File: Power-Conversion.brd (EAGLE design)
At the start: 182.9 x 114.3 mm, 46 parts, among them Q1 SUM90P10-19L, U7 LM2678

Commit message: Stuff
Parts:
- moved U$7 2.04 mm to (163.3, 28.1)
- moved U$5 0.38 mm to (162.4, 33.5)
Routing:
- net ON/OFF: track 169.5 -> 173.3 mm
- net N$10: track 6.11 -> 7.96 mm
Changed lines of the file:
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@@
 <attribute name="PN-DIGI" value="BZX84C22LT1GOSCT-ND" x="165.1" y="19.05" size="1.778" layer="27" rot="R180" display="off"/>
 </element>
-<element name="U$5" library="MotherboardParts" package="SOT23-3" value="5V" x="162.052" y="33.528" rot="R90"/>
+<element name="U$5" library="MotherboardParts" package="SOT23-3" value="5V" x="162.433" y="33.528" rot="R90"/>
 <element name="U$6" library="MotherboardParts" package="SOT23-3" value="22V" x="164.084" y="15.24" rot="R180">
 <attribute name="PN-DIGI" value="BZX84C22LT1GOSCT-ND" x="164.084" y="15.24" size="1.778" layer="27" rot="R180" display="off"/>
 </element>
-<element name="U$7" library="MotherboardParts" package="DPAK" value="NMOSFET-DPAK" x="161.29" y="28.194" rot="R90">
-<attribute name="PN-DIGI" value="497-4329-1-ND" x="161.29" y="28.194" size="1.778" layer="27" rot="R90" display="off"/>
-<attribute name="VDSS" value="60V" x="161.29" y="28.194" size="1.778" layer="27" rot="R90" display="off"/>
+<element name="U$7" library="MotherboardParts" package="DPAK" value="NMOSFET-DPAK" x="163.322" y="28.067" rot="R90">
+<attribute name="PN-DIGI" value="497-4329-1-ND" x="163.322" y="28.067" size="1.778" layer="27" rot="R90" display="off"/>
+<attribute name="VDSS" value="60V" x="163.322" y="28.067" size="1.778" layer="27" rot="R90" display="off"/>
 </element>
 <element name="U$9" library="PowerComponents" package="DPAK-3" value="SWITCHMODE_SCHOTTKY" x="8.382" y="58.42" rot="MR270"/>
@@
 <wire x1="181.356" y1="23.114" x2="181.356" y2="24.384" width="0.6096" layer="16"/>
 <via x="181.356" y="24.384" extent="1-16" drill="0.35"/>
-<wire x1="181.356" y1="24.384" x2="181.356" y2="26.924" width="0.6096" layer="1"/>
-<wire x1="181.356" y1="26.924" x2="180.086" y2="28.194" width="0.6096" layer="1"/>
 <via x="180.086" y="31.242" extent="1-16" drill="0.35"/>
-<wire x1="180.086" y1="28.194" x2="180.086" y2="31.242" width="0.6096" layer="1"/>
 <polygon width="0.4064" layer="16">
 <vertex x="28.448" y="96.52"/>
@@
 <contactref element="U$8" pad="P$11"/>
 <contactref element="U$8" pad="P$10"/>
+<wire x1="181.356" y1="27.94" x2="180.086" y2="29.21" width="0.6096" layer="1"/>
+<wire x1="180.086" y1="29.21" x2="180.086" y2="31.242" width="0.6096" layer="1"/>
+<wire x1="181.356" y1="24.384" x2="181.356" y2="27.94" width="0.6096" layer="1"/>
 </signal>
 <signal name="N$9">
@@
 <contactref element="R1" pad="2"/>
 <contactref element="U$7" pad="1"/>
-<wire x1="166.6" y1="25.914" x2="166.028" y2="25.342" width="0.8128" layer="1"/>
-<wire x1="166.028" y1="25.342" x2="166.028" y2="22.352" width="0.8128" layer="1"/>
 <wire x1="166.028" y1="22.352" x2="166.028" y2="20.072" width="0.8128" layer="1"/>
 <wire x1="166.028" y1="20.072" x2="166.05" y2="20.05" width="0.8128" layer="1"/>
+<wire x1="165.989" y1="22.391" x2="166.028" y2="22.352" width="0.4064" layer="1"/>
+<wire x1="168.632" y1="25.787" x2="168.626" y2="25.781" width="0.8128" layer="1"/>
+<wire x1="168.626" y1="25.781" x2="166.751" y2="25.781" width="0.8128" layer="1"/>
+<wire x1="166.751" y1="25.781" x2="165.989" y2="25.019" width="0.8128" layer="1"/>
+<wire x1="165.989" y1="25.019" x2="165.989" y2="22.391" width="0.8128" layer="1"/>
 </signal>
 <signal name="+5V">
@@
 <vertex x="179.578" y="14.224"/>
 <vertex x="179.832" y="14.478"/>
-<vertex x="179.832" y="27.178"/>
-<vertex x="176.022" y="27.178"/>
-<vertex x="170.434" y="32.766"/>
+<vertex x="180.086" y="28.194"/>
+<vertex x="173.863" y="35.052"/>
 <vertex x="169.926" y="33.274"/>
-<vertex x="162.306" y="33.274"/>
-<vertex x="162.306" y="31.75"/>
-<vertex x="164.084" y="29.972"/>
+<vertex x="163.068" y="33.274"/>
+<vertex x="163.068" y="31.75"/>
+<vertex x="164.719" y="31.75"/>
+<vertex x="164.846" y="31.623"/>
 <vertex x="164.846" y="29.21"/>
 <vertex x="167.386" y="29.21"/>
 <vertex x="169.418" y="27.178"/>
-<vertex x="169.418" y="23.622"/>
-<vertex x="167.894" y="23.622"/>
+<vertex x="170.561" y="27.305"/>
+<vertex x="170.561" y="24.765"/>
+<vertex x="170.434" y="24.638"/>
 </polygon>
 <via x="140.462" y="4.318" extent="1-16" drill="0.35"/>
@@
 <wire x1="139.192" y1="3.302" x2="139.192" y2="2.032" width="0.8128" layer="1"/>
 <polygon width="0.4064" layer="1">
-<vertex x="35.052" y="23.368"/>
+<vertex x="35.052" y="24.13"/>
 <vertex x="35.052" y="12.954"/>
 <vertex x="35.306" y="12.7"/>
 <vertex x="155.448" y="12.7"/>
-<vertex x="156.718" y="13.97"/>
-<vertex x="159.004" y="16.256"/>
-<vertex x="159.004" y="17.526"/>
+<vertex x="157.988" y="12.954"/>
+<vertex x="159.004" y="13.97"/>
 <vertex x="159.004" y="22.86"/>
-<vertex x="155.448" y="26.416"/>
-<vertex x="155.448" y="32.258"/>
-<vertex x="159.258" y="36.068"/>
+<vertex x="157.988" y="26.416"/>
+<vertex x="157.988" y="32.258"/>
 <vertex x="159.512" y="36.322"/>
 <vertex x="164.338" y="36.322"/>
 <vertex x="164.338" y="32.766"/>
 <vertex x="169.164" y="32.766"/>
-<vertex x="173.482" y="28.448"/>
-<vertex x="173.482" y="42.164"/>
-<vertex x="158.75" y="42.164"/>
-<vertex x="151.638" y="35.052"/>
+<vertex x="174.879" y="28.448"/>
+<vertex x="174.879" y="42.164"/>
+<vertex x="146.431" y="42.164"/>
+<vertex x="146.431" y="29.464"/>
+<vertex x="151.638" y="24.257"/>
 <vertex x="151.638" y="19.05"/>
 <vertex x="151.384" y="18.796"/>
@@
 <vertex x="39.878" y="18.796"/>
 <vertex x="39.878" y="24.13"/>
-<vertex x="35.052" y="24.13"/>
 </polygon>
 <contactref element="U$20" pad="48V_GND4"/>
@@
 <contactref element="R2" pad="1"/>
 <contactref element="U$5" pad="3"/>
-<wire x1="160.952" y1="33.528" x2="160.952" y2="29.444" width="0.6096" layer="1"/>
-<wire x1="159.988" y1="28.48" x2="160.952" y2="29.444" width="0.6096" layer="1"/>
-<wire x1="159.988" y1="28.48" x2="159.702" y2="28.194" width="0.6096" layer="1"/>
-<wire x1="160.782" y1="15.836" x2="160.782" y2="27.686" width="0.6096" layer="1"/>
+<wire x1="160.952" y1="29.444" x2="159.988" y2="28.48" width="0.6096" layer="1"/>
+<wire x1="159.988" y1="28.48" x2="161.734" y2="28.067" width="0.6096" layer="1"/>
 <wire x1="160.782" y1="27.686" x2="159.988" y2="28.48" width="0.6096" layer="1"/>
-<wire x1="159.702" y1="28.194" x2="159.702" y2="24.828" width="0.4064" layer="1"/>
-<wire x1="159.702" y1="24.828" x2="159.258" y2="24.384" width="0.4064" layer="1"/>
 <via x="159.258" y="24.384" extent="1-16" drill="0.35"/>
 <wire x1="159.258" y1="24.384" x2="152.908" y2="24.384" width="0.4064" layer="16"/>
@@
 <wire x1="33.4344" y1="24.2904" x2="42.1156125" y2="24.2904" width="0.4064" layer="16"/>
 <wire x1="42.4632125" y1="24.638" x2="55.626" y2="24.638" width="0.4064" layer="16"/>
+<wire x1="159.702" y1="26.606" x2="160.782" y2="27.686" width="0.4064" layer="1"/>
+<wire x1="160.782" y1="25.908" x2="160.782" y2="27.686" width="0.4064" layer="1"/>
+<wire x1="159.258" y1="24.384" x2="160.782" y2="25.908" width="0.4064" layer="1"/>
+<wire x1="160.782" y1="15.836" x2="160.782" y2="24.13" width="0.4064" layer="1"/>
+<wire x1="161.734" y1="25.082" x2="161.734" y2="28.067" width="0.4064" layer="1"/>
+<wire x1="160.782" y1="24.13" x2="161.734" y2="25.082" width="0.4064" layer="1"/>
+<wire x1="161.333" y1="33.528" x2="161.333" y2="29.825" width="0.4064" layer="1"/>
+<wire x1="161.333" y1="29.825" x2="160.952" y2="29.444" width="0.4064" layer="1"/>
 </signal>
 <signal name="+12V_1">

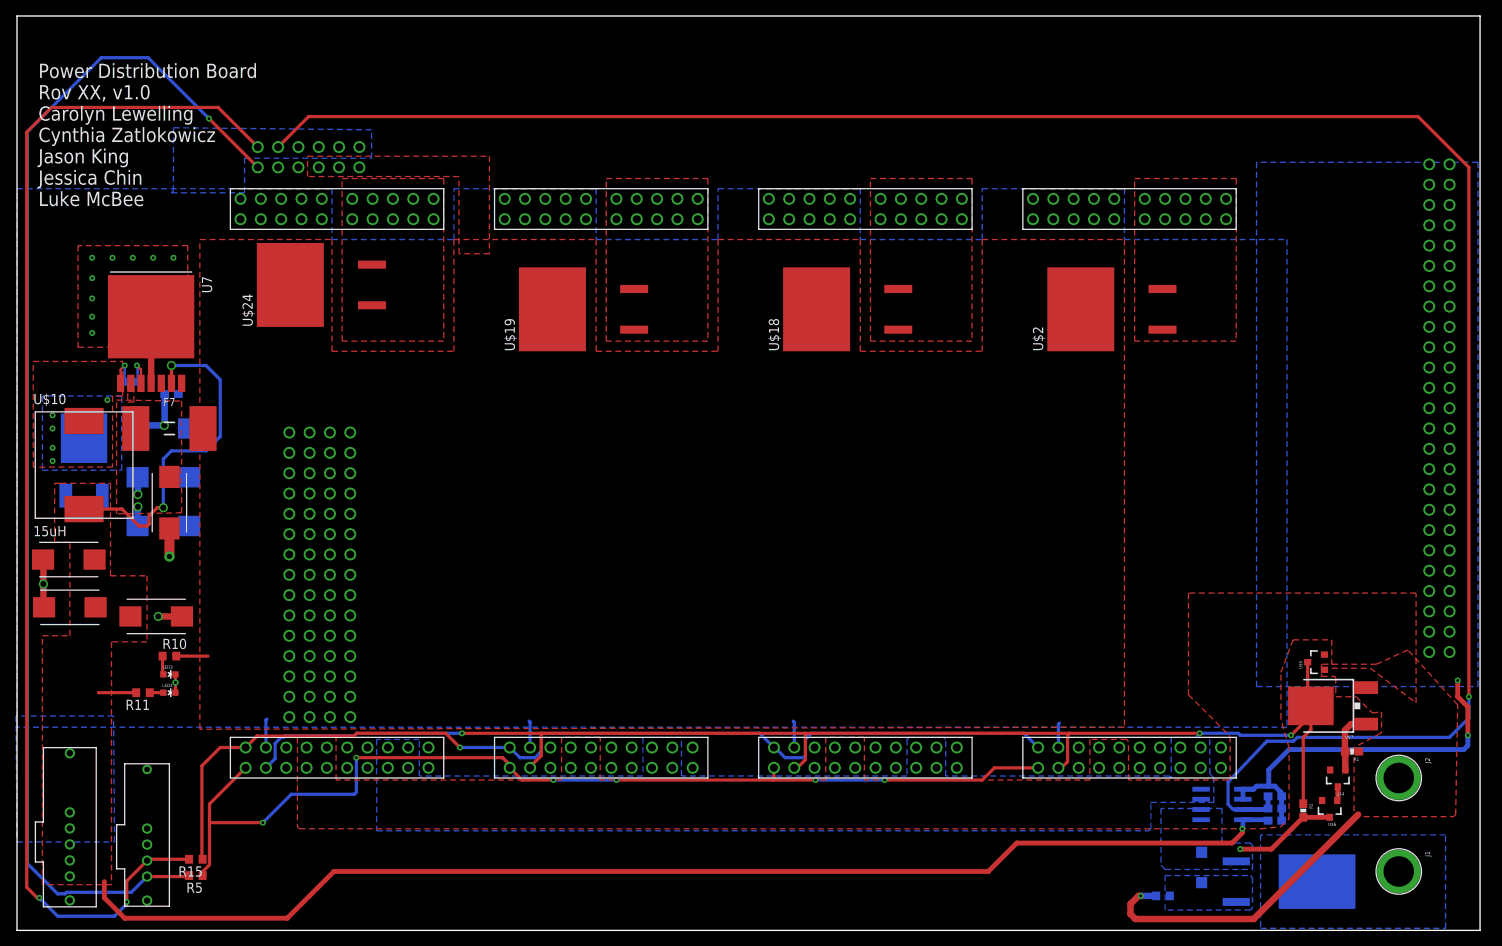
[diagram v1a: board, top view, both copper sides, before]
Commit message: Fixed trace widths for +48V and GND
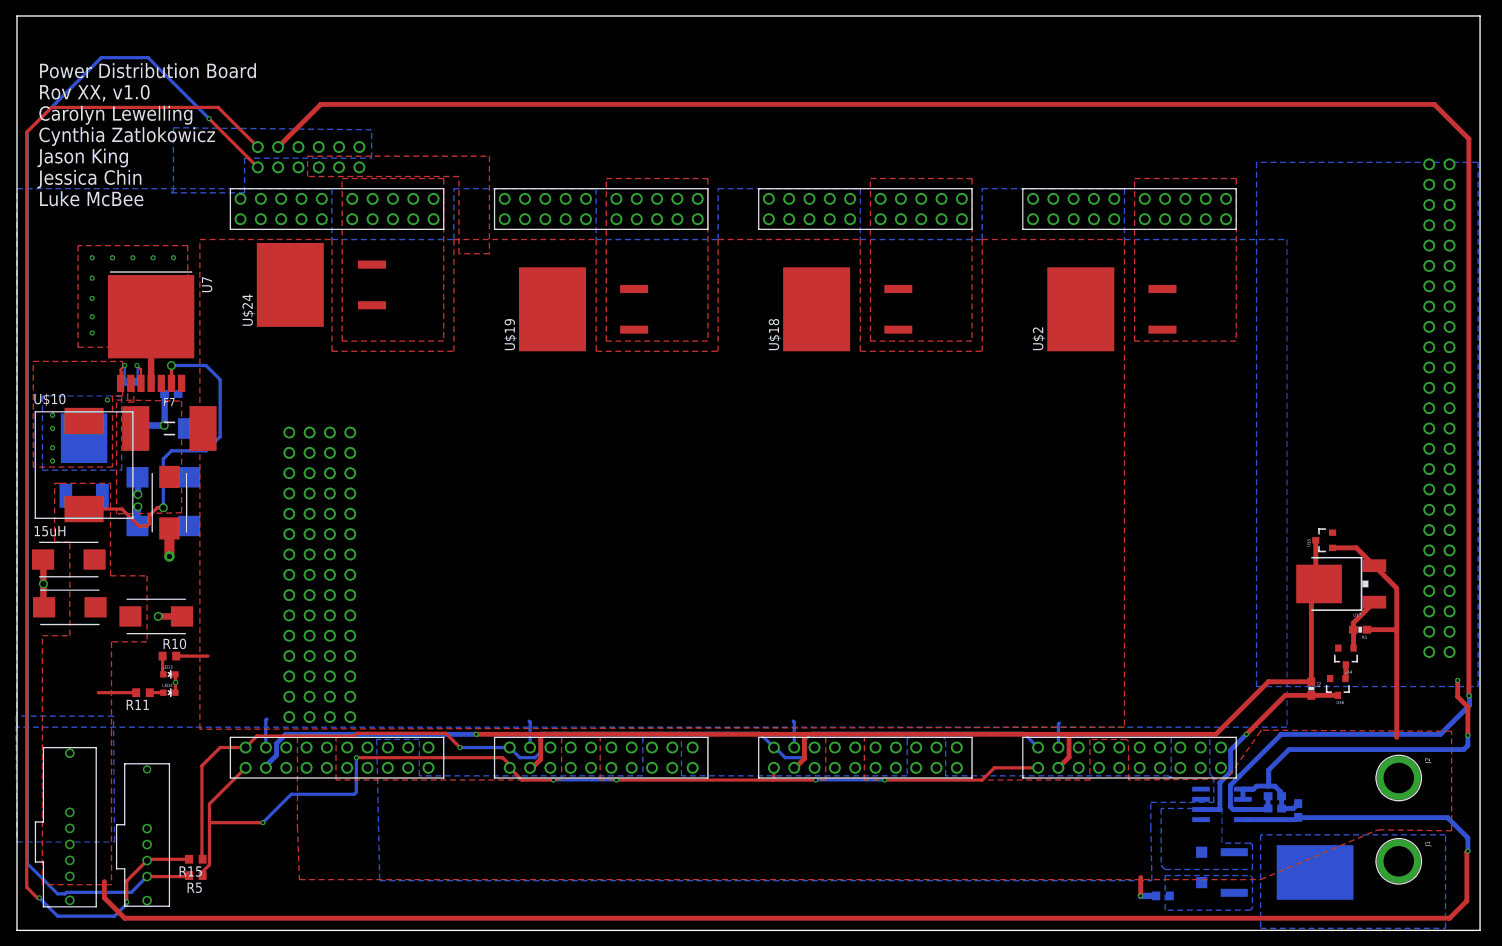
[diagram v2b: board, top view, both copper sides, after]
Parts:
- moved U$5 15.3 mm to (163.4, 48.8)
- moved U$7 15.3 mm to (164.3, 43.3)
- moved U$6 15.3 mm to (165.1, 30.5)
- moved R1 15.3 mm to (167.9, 37.6)
- moved R2 15.3 mm to (161.8, 30.2)
- moved U$4 15.3 mm to (166.1, 34.3)
- moved C1 3.19 mm to (160.1, 15.0), turned to 270 degrees
- moved J1 1.27 mm to (172.7, 8.64)
- moved Q1 1.17 mm to (158.8, 7.24)
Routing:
- net +5V: track 202.3 -> 259.1 mm
- net +48V: track 12.8 -> 26.6 mm
- net ON/OFF: track 173.3 -> 168.9 mm, vias 3 -> 1
- net 48_I_ANALOG: track 265.1 -> 268.0 mm
- net 48V_GND: track 39.0 -> 36.8 mm
- net N$10: track 7.96 -> 6.82 mm
- net GND: track 83.5 -> 84.3 mm

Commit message: Cleaning up
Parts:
- added JP1, JP2: (no value), pinhead:1X01
- moved R15 2.33 mm to (24.5, 9.78)
- moved R5 2.16 mm to (24.5, 6.73)
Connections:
- net SCL: now also JP1.1
- net SDA: now also JP2.1
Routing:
- net SCL1: track 128.7 -> 123.5 mm
- net SDA1: track 126.2 -> 122.5 mm
- net SDA: track 153.0 -> 155.5 mm
- net SCL: track 152.5 -> 154.7 mm
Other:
- board text added: "+48V"
- board text added: "GND"
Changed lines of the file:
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@@
 Jessica Chin
 Luke McBee</text>
+<text x="176.403" y="18.415" size="1.778" layer="21">GND</text>
+<text x="176.149" y="7.112" size="1.778" layer="21">+48V</text>
 </plain>
 <attributes>
@@
 <attribute name="SPICEPREFIX" value="B" x="38.354" y="75.438" size="1.778" layer="27" rot="R90" display="off"/>
 </element>
-<element name="R15" library="resistor" package="R0603" value="0R" x="22.352" y="8.89" rot="R180"/>
-<element name="R5" library="resistor" package="R0603" value="0R" x="22.352" y="6.858" rot="R180"/>
+<element name="R15" library="resistor" package="R0603" value="0R" x="24.511" y="9.779" rot="R180"/>
+<element name="R5" library="resistor" package="R0603" value="0R" x="24.511" y="6.731" rot="R180"/>
 <element name="U$11" library="BackplaneParts" package="T2I5P" value="T2I5P" x="3.302" y="3.048" rot="R270"/>
 <element name="U$12" library="BackplaneParts" package="T2I" value="T2I" x="13.462" y="20.828" rot="R270"/>
@@
 <element name="F7" library="PowerComponents" package="PTC-2920" value="10A" x="19.05" y="62.738"/>
 <element name="U$8" library="MotherboardParts" package="ESC-FULL" value="ESC-FULL" x="36.449" y="96.647"/>
+<element name="JP1" library="pinhead" library_urn="urn:adsk.eagle:library:325" package="1X01" package3d_urn="urn:adsk.eagle:package:22485/2" value="" x="20.955" y="6.731"/>
+<element name="JP2" library="pinhead" library_urn="urn:adsk.eagle:library:325" package="1X01" package3d_urn="urn:adsk.eagle:package:22485/2" value="" x="20.955" y="9.779"/>
 </elements>
 <signals>
@@
 <contactref element="R5" pad="2"/>
 <contactref element="U$12" pad="4"/>
-<wire x1="21.502" y1="6.858" x2="21.372" y2="6.728" width="0.4064" layer="1"/>
-<wire x1="21.372" y1="6.728" x2="16.262" y2="6.728" width="0.4064" layer="1"/>
 <wire x1="1.27" y1="8.382" x2="5.08" y2="4.572" width="0.4064" layer="16"/>
 <wire x1="5.08" y1="4.572" x2="5.99820625" y2="4.572" width="0.4064" layer="16"/>
@@
 <wire x1="24.003" y1="101.473" x2="16.383" y2="109.093" width="0.4064" layer="16"/>
 <wire x1="30.099" y1="95.377" x2="24.003" y2="101.473" width="0.4064" layer="1"/>
+<contactref element="JP1" pad="1"/>
+<wire x1="16.262" y1="6.728" x2="20.952" y2="6.728" width="0.4064" layer="1"/>
+<wire x1="20.952" y1="6.728" x2="20.955" y2="6.731" width="0.4064" layer="1"/>
+<wire x1="20.955" y1="6.731" x2="23.661" y2="6.731" width="0.4064" layer="1"/>
 </signal>
 <signal name="SDA">
 <contactref element="R15" pad="2"/>
 <contactref element="U$12" pad="3"/>
-<wire x1="21.502" y1="8.89" x2="16.424" y2="8.89" width="0.4064" layer="1"/>
-<wire x1="16.424" y1="8.89" x2="16.262" y2="8.728" width="0.4064" layer="1"/>
 <wire x1="16.262" y1="8.728" x2="13.716" y2="6.182" width="0.4064" layer="1"/>
 <wire x1="13.716" y1="6.182" x2="13.716" y2="3.556" width="0.4064" layer="1"/>
@@
 <wire x1="30.099" y1="97.917" x2="25.146" y2="102.87" width="0.4064" layer="1"/>
 <wire x1="25.146" y1="102.87" x2="4.318" y2="102.87" width="0.4064" layer="1"/>
+<contactref element="JP2" pad="1"/>
+<wire x1="16.262" y1="8.728" x2="17.313" y2="9.779" width="0.4064" layer="1"/>
+<wire x1="17.313" y1="9.779" x2="20.955" y2="9.779" width="0.4064" layer="1"/>
+<wire x1="20.955" y1="9.779" x2="23.661" y2="9.779" width="0.4064" layer="1"/>
 </signal>
 <signal name="48_I_ANALOG">
@@
 <wire x1="30.0054" y1="24.2904" x2="28.575" y2="22.86" width="0.4064" layer="1"/>
 <wire x1="42.1156125" y1="24.2904" x2="30.0054" y2="24.2904" width="0.4064" layer="1"/>
-<wire x1="28.575" y1="22.86" x2="25.4" y2="22.86" width="0.4064" layer="1"/>
-<wire x1="25.4" y1="22.86" x2="23.114" y2="20.574" width="0.4064" layer="1"/>
-<wire x1="23.114" y1="8.978" x2="23.202" y2="8.89" width="0.4064" layer="1"/>
-<wire x1="23.114" y1="20.574" x2="23.114" y2="8.978" width="0.4064" layer="1"/>
+<wire x1="25.361" y1="9.779" x2="25.361" y2="19.646" width="0.4064" layer="1"/>
+<wire x1="25.361" y1="19.646" x2="28.575" y2="22.86" width="0.4064" layer="1"/>
 </signal>
 <signal name="SCL1">
@@
 <contactref element="R5" pad="1"/>
 <contactref element="U$23" pad="SCL"/>
-<wire x1="23.202" y1="6.858" x2="23.202" y2="7.33710625" width="0.4064" layer="1"/>
-<wire x1="23.202" y1="7.33710625" x2="24.0576" y2="8.19270625" width="0.4064" layer="1"/>
-<wire x1="24.0576" y1="15.8026" x2="28.575" y2="20.32" width="0.4064" layer="1"/>
-<wire x1="24.0576" y1="8.19270625" x2="24.0576" y2="13.462" width="0.4064" layer="1"/>
-<wire x1="24.0576" y1="13.462" x2="24.0576" y2="15.8026" width="0.4064" layer="1"/>
 <via x="30.734" y="13.462" extent="1-16" drill="0.35"/>
 <wire x1="30.734" y1="13.462" x2="34.29" y2="17.018" width="0.4064" layer="16"/>
@@
 <wire x1="60.706" y1="21.59" x2="61.595" y2="20.701" width="0.4064" layer="1"/>
 <wire x1="61.595" y1="20.701" x2="61.595" y2="20.32" width="0.4064" layer="1"/>
-<wire x1="24.0576" y1="13.462" x2="30.734" y2="13.462" width="0.4064" layer="1"/>
 <wire x1="42.418" y1="17.272" x2="42.418" y2="21.59" width="0.4064" layer="16"/>
 <wire x1="42.418" y1="21.59" x2="60.706" y2="21.59" width="0.4064" layer="1"/>
@@
 <wire x1="94.488" y1="18.796" x2="99.822" y2="18.796" width="0.4064" layer="1"/>
 <wire x1="99.822" y1="18.796" x2="108.458" y2="18.796" width="0.4064" layer="16"/>
+<wire x1="28.575" y1="20.32" x2="28.575" y2="13.462" width="0.4064" layer="1"/>
+<wire x1="28.575" y1="13.462" x2="30.734" y2="13.462" width="0.4064" layer="1"/>
+<wire x1="28.575" y1="13.462" x2="28.575" y2="9.945" width="0.4064" layer="1"/>
+<wire x1="28.575" y1="9.945" x2="25.361" y2="6.731" width="0.4064" layer="1"/>
 </signal>
 <signal name="N$2">
@@
 which will not be processed correctly with this version.
 </note>
+<note version="8.2" severity="warning">
+Since Version 8.2, EAGLE supports online libraries. The ids
+of those online libraries will not be understood (or retained)
+with this version.
+</note>
+<note version="8.3" severity="warning">
+Since Version 8.3, EAGLE supports URNs for individual library
+assets (packages, symbols, and devices). The URNs of those assets
+will not be understood (or retained) with this version.
+</note>
+<note version="8.3" severity="warning">
+Since Version 8.3, EAGLE supports the association of 3D packages
+with devices in libraries, schematics, and board files. Those 3D
+packages will not be understood (or retained) with this version.
+</note>
 </compatibility>

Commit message: Version submitted to elecrow
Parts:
- added J3: (no value), SparkFun-Connectors:BANANA_CONN
- moved U$11 6.98 mm to (3.30, 10.0)
- moved U$24 3.06 mm to (38.1, 72.4)
- moved U$15 2.54 mm to (6.35, 120.7)
- moved J2 1.40 mm to (172.7, 17.7)
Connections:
- net VCC: now also J3.P$1
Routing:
- net +5V: track 259.1 -> 271.2 mm
